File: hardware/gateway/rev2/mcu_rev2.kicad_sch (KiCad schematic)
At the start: 31 parts, among them IC1 STM8L151K4T6, IC5 MB85RC64TAPNF-G-BDERE1, J1 G8250041000YEU, J2 M20-9770342, Q1 IRLML6402TRPBF, U1 2462

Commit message: EG-59 Adapted the buzzer driver.
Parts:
- added LS1: PKMCS1818E20A0-R1, MyParts:PKMCS1818E20A0R1, symbol PKMCS1818E20A0-R1:PKMCS1818E20A0-R1
- added R18, R19: 100R, Resistor_SMD:R_0603_1608Metric, symbol Device:R_US
- added R20: 10K, Resistor_SMD:R_0603_1608Metric, symbol Device:R_US
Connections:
- net BZR_N: now also R19.2
- net BZR_P: now also R18.2
- net BZR_EN: no longer names the net of IC1.29 (PC4)
- new net: LS1.1 (+_1), LS1.2 (+_2), R18.1, R20.2
- new net: LS1.3 (-_1), LS1.4 (-_2), R19.1, R20.1
- no-connect marks 12 -> 13
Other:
- moved on the sheet: C7, C8, IC5, LED1, LED2, LED3, R10, R11, R12, R8, R9

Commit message: EG-59 Schematic with the needed components, plus PCB.
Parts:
- removed C1, C2: 100nF, Capacitor_SMD:C_0603_1608Metric, symbol Device:C
- removed C6: 47uF, 6.3V, Capacitor_SMD:C_1206_3216Metric, symbol Device:C
- removed J1: G8250041000YEU, MyParts:HDRV4W55P0X200_1X4_800X200X635P, symbol G8250041000YEU:G8250041000YEU
- removed Q1: IRLML6402TRPBF, MyParts:SOT95P237X112-3N, symbol IRLML6402TRPBF:IRLML6402TRPBF
- removed R1, R3: 100K, Resistor_SMD:R_0603_1608Metric, symbol Device:R_US
- removed R2, R5: 1M, Resistor_SMD:R_0603_1608Metric, symbol Device:R_US
- removed R4: 10K, Resistor_SMD:R_0603_1608Metric, symbol Device:R_US
- removed R6: 510K, Resistor_SMD:R_0603_1608Metric, symbol Device:R_US
- removed R7: 1K, Resistor_SMD:R_0603_1608Metric, symbol Device:R_US
- removed S1: MASM-14R-8-10, MyParts:MASM14R810, symbol MASM-14R-8-10:MASM-14R-8-10
- removed S2: TL6120DF160QG, MyParts:TL6120DF160QG, symbol TL6120DF160QG:TL6120DF160QG
- removed U1: 2462, MyParts:2462, symbol 2462:2462
- added CLK1: SPI_CK, TestPoint:TestPoint_Pad_D1.0mm, symbol Connector:TestPoint
- added CS1: SPI_CS, TestPoint:TestPoint_Pad_D1.0mm, symbol Connector:TestPoint
- added GD1: GD0, TestPoint:TestPoint_Pad_D1.0mm, symbol Connector:TestPoint
- added J1: 22-28-4044, MyParts:HDRV4W66P0X254_1X4_1016X249X1067P, symbol 22-28-4044:22-28-4044
- added LED_B1, LED_R1, LED_Y1: LED, TestPoint:TestPoint_Pad_D1.0mm, symbol Connector:TestPoint
- added MCUVDD1: MCU_VDD, TestPoint:TestPoint_Pad_D1.0mm, symbol Connector:TestPoint
- added MISO1: SPI_MISO, TestPoint:TestPoint_Pad_D1.0mm, symbol Connector:TestPoint
- added MOSI1: SPI_MOSI, TestPoint:TestPoint_Pad_D1.0mm, symbol Connector:TestPoint
- added S3: PTS810SJK250SMTR_LFS, MyParts:PTS810SJK250SMTRLFS, symbol PTS810SJK250SMTR_LFS:PTS810SJK250SMTR_LFS
- added U1: IRM-01-3.3, MyParts:IRM-01-3-3, symbol IRM-01-3-3:IRM-01-3.3
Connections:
- net BTN: now also S3.2 (NO_2)
- net CS: now also CS1.1
- net GND: now also J2.1, J1.3, S3.4 (COM_2); no longer J2.3
- net IRQ: now also GD1.1
- net LED_B: now also LED_B1.1
- net LED_R: now also LED_R1.1
- net LED_Y: now also LED_Y1.1
- net NRST: now also J1.4
- net SCLK: now also CLK1.1
- net SDI: now also MOSI1.1
- net SDO: now also MISO1.1
- net SWIM: now also J1.2
- net TX: now also J2.3; no longer J2.1
- net VDD: now also J1.1, MCUVDD1.1
- net DOOR: no longer names the net of IC1.22 (PD5)
- net V_MEAS: no longer names the net of IC1.6 (PA6)
- no-connect marks 13 -> 15
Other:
- note added: "Insert test points. Insert holes for screws. Check the MCU pins again, for pull-ups, etc. Change the LEDs. Change all components to JLCPCB stock."
- note added: "Use internal MCU pull-up. ~45 Kohms"
- moved on the sheet: C3, C4, C5, C7, C8, IC1, IC5, J2, R11, R12

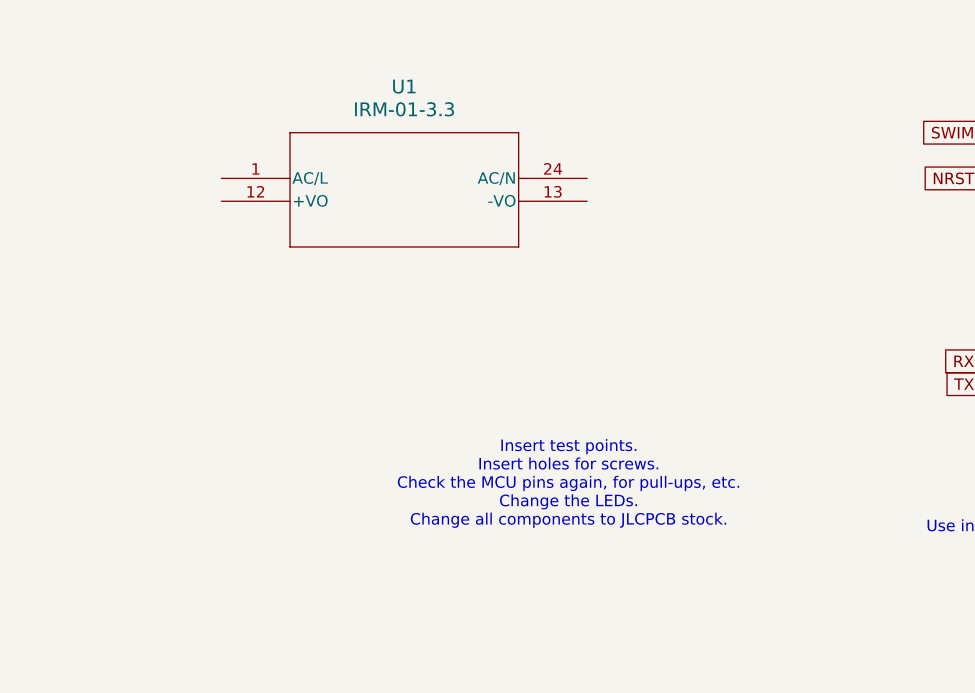
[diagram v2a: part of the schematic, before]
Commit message: EG-59 First mechanical project with the AC-DC component and buzzer.
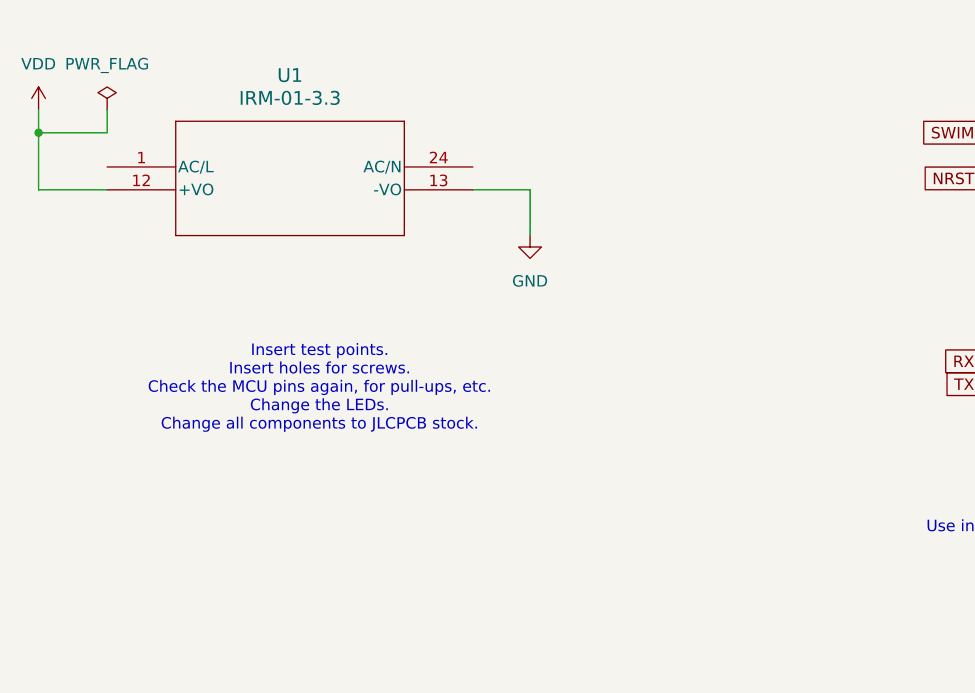
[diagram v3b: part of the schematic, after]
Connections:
- net GND: now also U1.13 (-VO)
- net VDD: now also U1.12 (+VO)
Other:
- moved on the sheet: U1

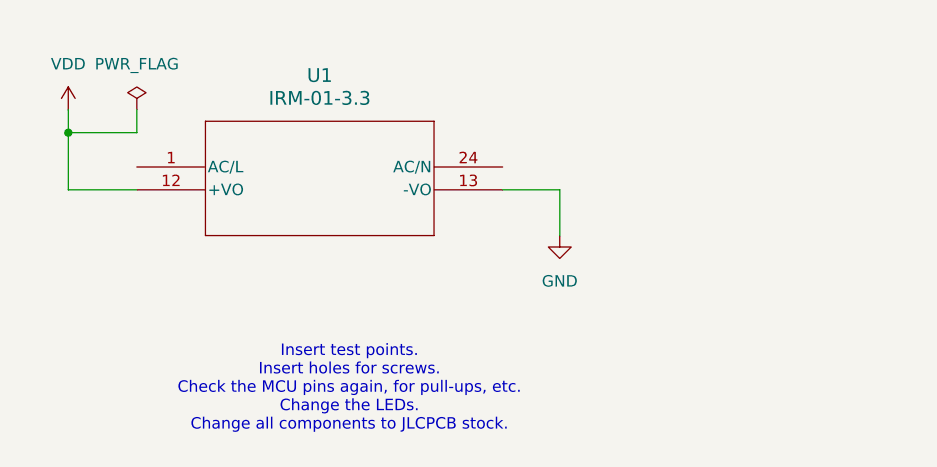
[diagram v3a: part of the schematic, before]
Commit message: EG-59 Correct position of AC-DC and buzzer in the PCB.
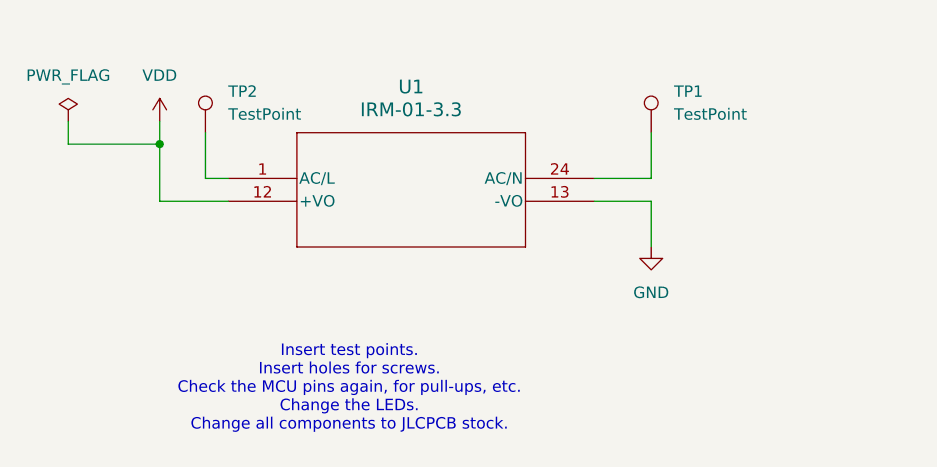
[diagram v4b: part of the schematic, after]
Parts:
- added TP1, TP2: TestPoint, TestPoint:TestPoint_Plated_Hole_D2.0mm, symbol Connector:TestPoint
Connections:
- net at U1.1 (AC/L): now also TP2.1
- net at U1.24 (AC/N): now also TP1.1
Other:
- moved on the sheet: U1

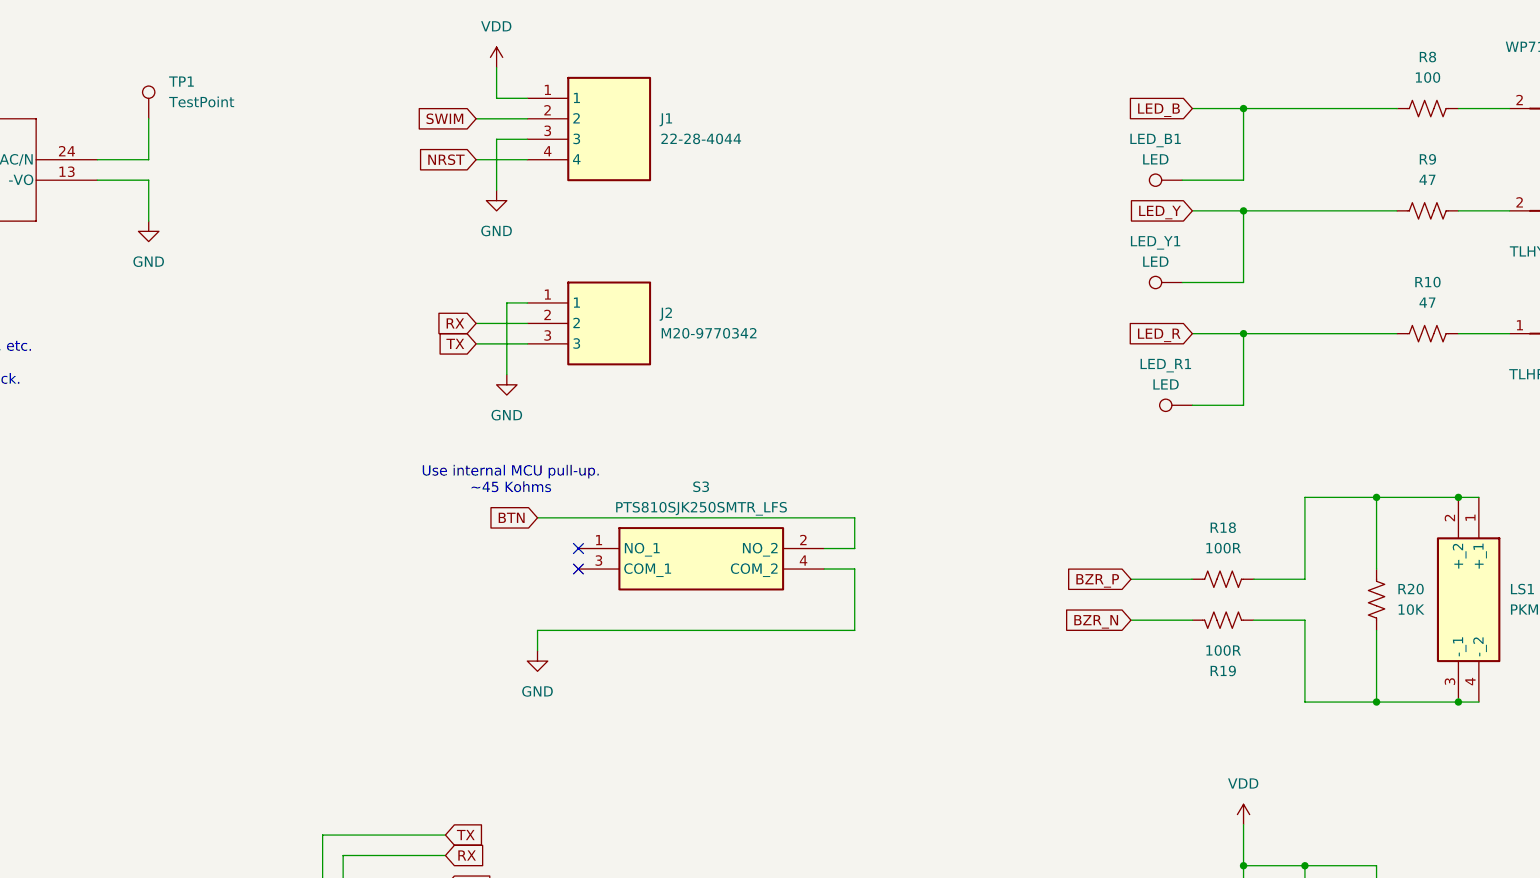
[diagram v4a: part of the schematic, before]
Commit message: EG-59 Antenna and headers fix, from schematic to 3D.
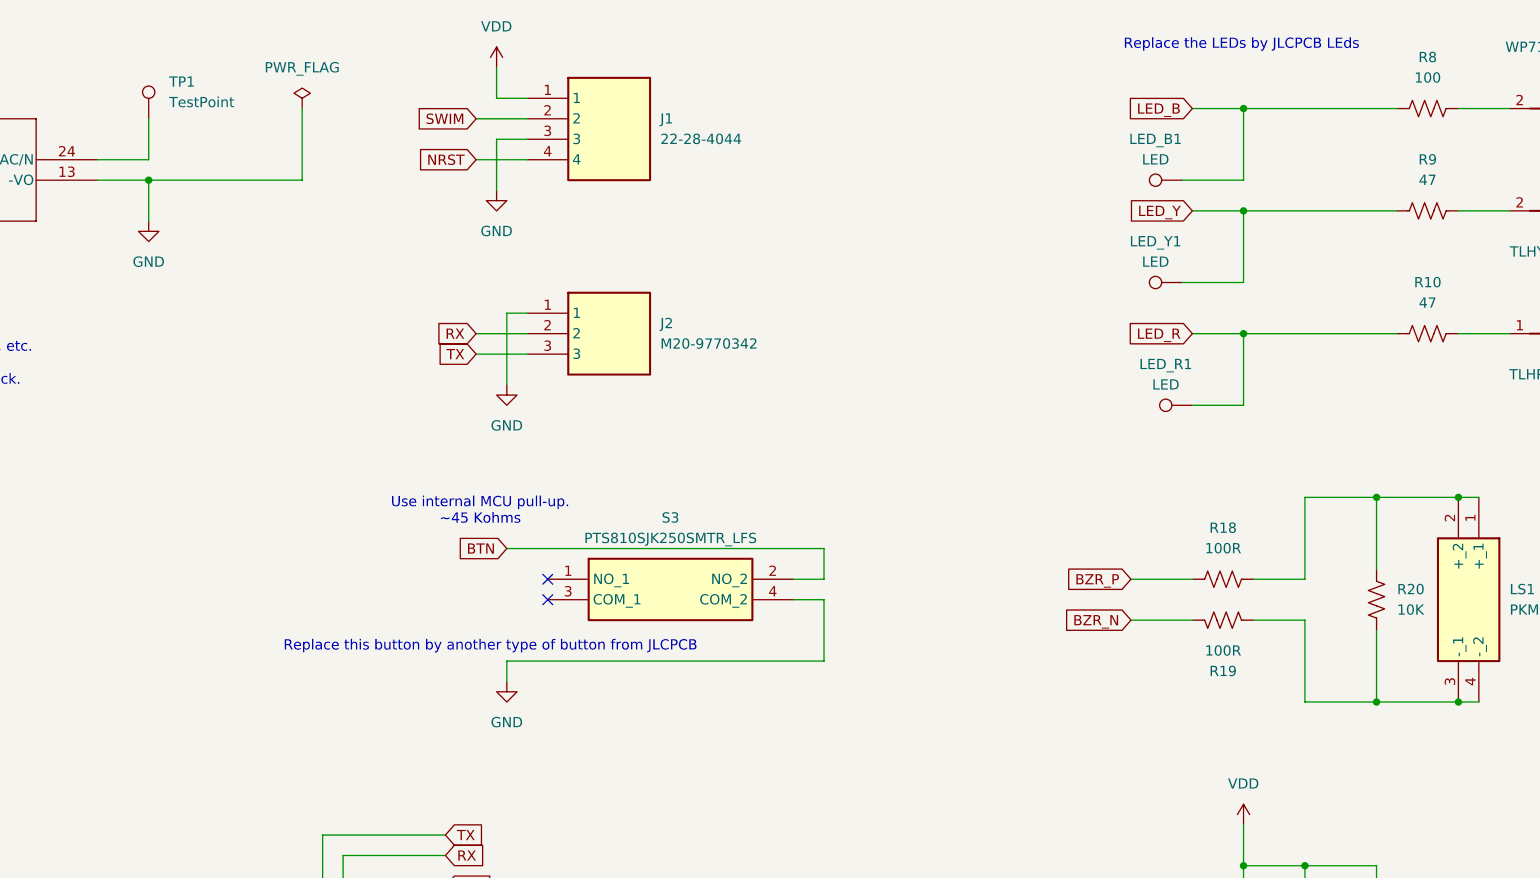
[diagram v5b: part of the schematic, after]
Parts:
- J1: Mouser Price/Stock https://pt.mouser.com/en/ProductDetail/Molex/22-28-4044?qs=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 -> https://www.mouser.com/Search/Refine.aspx?Keyword=538-22-28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
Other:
- note added: "Replace the LEDs by JLCPCB LEds"
- note added: "Replace this button by another type of button from JLCPCB"
- moved on the sheet: J2, S3

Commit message: EG-59 Schematic finished.
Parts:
- removed S3: PTS810SJK250SMTR_LFS, MyParts:PTS810SJK250SMTRLFS, symbol PTS810SJK250SMTR_LFS:PTS810SJK250SMTR_LFS
- removed TP1, TP2: TestPoint, TestPoint:TestPoint_Plated_Hole_D2.0mm, symbol Connector:TestPoint
- added J_L1, J_N1: (no value), MyParts:230V, symbol pad-hole:230V
- added S1: TS02-66-100-BK-160-SCR-D, MyParts:TS0266100BK100LCRD, symbol TS02-66-100-BK-160-SCR-D:TS02-66-100-BK-160-SCR-D
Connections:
- net BTN: now also S1.3 (COM_1)
- net GND: now also S1.1 (NO_1)
- net at U1.1 (AC/L): now also J_L1.1 (V)
- net at U1.24 (AC/N): now also J_N1.1 (V)
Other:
- note added: "Check the MCU pins again, for pull-ups, etc."
- note removed: "Insert test points. Insert holes for screws. Check the MCU pins again, for pull-ups, etc. Change the LEDs. Change all components to JLCPCB stock."
- note removed: "Replace the LEDs by JLCPCB LEds"
- note removed: "Replace this button by another type of button from JLCPCB"
- moved on the sheet: J1, J2, U1

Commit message: EG-59 RF components place defined.
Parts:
- renumbered C3 to C1, C4 to C2, C5 to C3, C7 to C4, C8 to C50
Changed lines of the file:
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@@
 		(dnp no)
 		(fields_autoplaced yes)
-		(property "Reference" "C4"
+		(property "Reference" "C2"
 			(at 45.72 167.6399 0)
 			(show_name no)
@@
 			(project "gateway_rev2"
 				(path "/d3cb7130-decc-418b-958e-e5d84a8d867f/ec220677-d66d-4ee1-961f-1c93fb46783a"
-					(reference "C4")
+					(reference "C2")
 					(unit 1)
 				)
@@
 		(dnp no)
 		(fields_autoplaced yes)
-		(property "Reference" "C3"
+		(property "Reference" "C1"
 			(at 68.58 144.7799 0)
 			(show_name no)
@@
 			(project "gateway_rev2"
 				(path "/d3cb7130-decc-418b-958e-e5d84a8d867f/ec220677-d66d-4ee1-961f-1c93fb46783a"
-					(reference "C3")
+					(reference "C1")
 					(unit 1)
 				)
@@
 		(dnp no)
 		(fields_autoplaced yes)
-		(property "Reference" "C7"
+		(property "Reference" "C4"
 			(at 264.16 140.9699 0)
 			(show_name no)
@@
 			(project "gateway_rev2"
 				(path "/d3cb7130-decc-418b-958e-e5d84a8d867f/ec220677-d66d-4ee1-961f-1c93fb46783a"
-					(reference "C7")
+					(reference "C4")
 					(unit 1)
 				)
@@
 		(dnp no)
 		(fields_autoplaced yes)
-		(property "Reference" "C5"
+		(property "Reference" "C3"
 			(at 66.04 167.6399 0)
 			(show_name no)
@@
 			(project "gateway_rev2"
 				(path "/d3cb7130-decc-418b-958e-e5d84a8d867f/ec220677-d66d-4ee1-961f-1c93fb46783a"
-					(reference "C5")
+					(reference "C3")
 					(unit 1)
 				)
@@
 		(dnp no)
 		(fields_autoplaced yes)
-		(property "Reference" "C8"
+		(property "Reference" "C50"
 			(at 276.86 140.9699 0)
 			(show_name no)
@@
 			(project "gateway_rev2"
 				(path "/d3cb7130-decc-418b-958e-e5d84a8d867f/ec220677-d66d-4ee1-961f-1c93fb46783a"
-					(reference "C8")
+					(reference "C50")
 					(unit 1)
 				)

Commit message: EG-59 RF Components placed. All passive components 0402.
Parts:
- C2, C3: footprint Capacitor_SMD:C_0603_1608Metric -> Capacitor_SMD:C_0402_1005Metric
- R10, R11, R12, R18, R19, R20, R8, R9: footprint Resistor_SMD:R_0603_1608Metric -> Resistor_SMD:R_0402_1005Metric
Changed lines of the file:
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@@
 			)
 		)
-		(property "Footprint" "Resistor_SMD:R_0603_1608Metric"
+		(property "Footprint" "Resistor_SMD:R_0402_1005Metric"
 			(at 230.124 126.746 90)
 			(hide yes)
@@
 			)
 		)
-		(property "Footprint" "Resistor_SMD:R_0603_1608Metric"
+		(property "Footprint" "Resistor_SMD:R_0402_1005Metric"
 			(at 220.726 89.154 90)
 			(hide yes)
@@
 			)
 		)
-		(property "Footprint" "Capacitor_SMD:C_0603_1608Metric"
+		(property "Footprint" "Capacitor_SMD:C_0402_1005Metric"
 			(at 42.8752 172.72 0)
 			(hide yes)
@@
 			)
 		)
-		(property "Footprint" "Resistor_SMD:R_0603_1608Metric"
+		(property "Footprint" "Resistor_SMD:R_0402_1005Metric"
 			(at 220.726 86.106 90)
 			(hide yes)
@@
 			)
 		)
-		(property "Footprint" "Resistor_SMD:R_0603_1608Metric"
+		(property "Footprint" "Resistor_SMD:R_0402_1005Metric"
 			(at 246.634 25.654 90)
 			(hide yes)
@@
 			)
 		)
-		(property "Footprint" "Resistor_SMD:R_0603_1608Metric"
+		(property "Footprint" "Resistor_SMD:R_0402_1005Metric"
 			(at 246.634 53.594 90)
 			(hide yes)
@@
 			)
 		)
-		(property "Footprint" "Resistor_SMD:R_0603_1608Metric"
+		(property "Footprint" "Resistor_SMD:R_0402_1005Metric"
 			(at 239.014 126.746 90)
 			(hide yes)
@@
 			)
 		)
-		(property "Footprint" "Resistor_SMD:R_0603_1608Metric"
+		(property "Footprint" "Resistor_SMD:R_0402_1005Metric"
 			(at 246.634 38.354 90)
 			(hide yes)
@@
 			)
 		)
-		(property "Footprint" "Capacitor_SMD:C_0603_1608Metric"
+		(property "Footprint" "Capacitor_SMD:C_0402_1005Metric"
 			(at 63.1952 172.72 0)
 			(hide yes)
@@
 			)
 		)
-		(property "Footprint" "Resistor_SMD:R_0603_1608Metric"
+		(property "Footprint" "Resistor_SMD:R_0402_1005Metric"
 			(at 239.014 87.376 90)
 			(hide yes)
